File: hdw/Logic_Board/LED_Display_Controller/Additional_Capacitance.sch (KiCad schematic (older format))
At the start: 3 parts

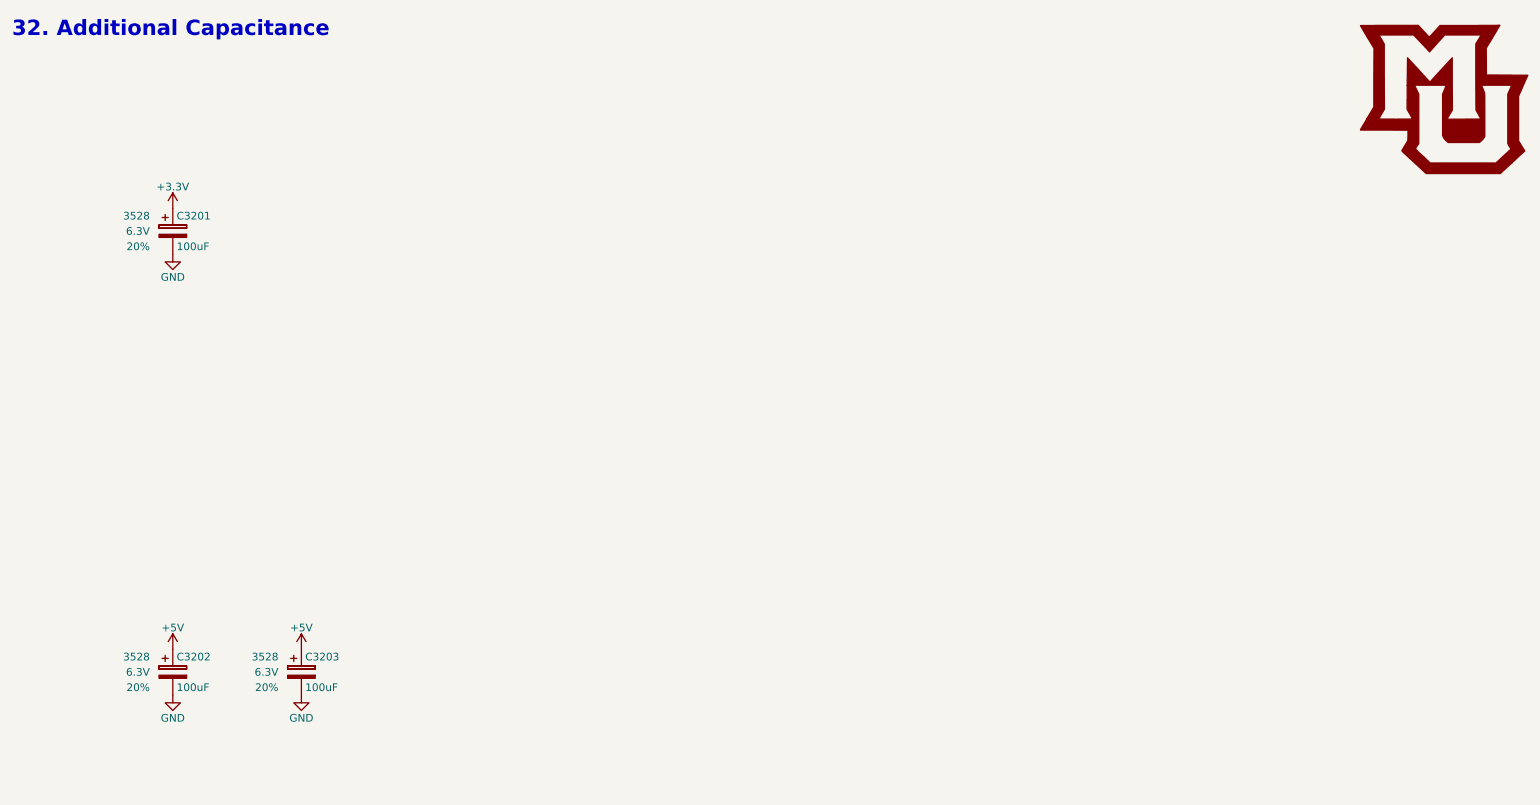
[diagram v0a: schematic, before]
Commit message: Added stitching caps, mor erouting
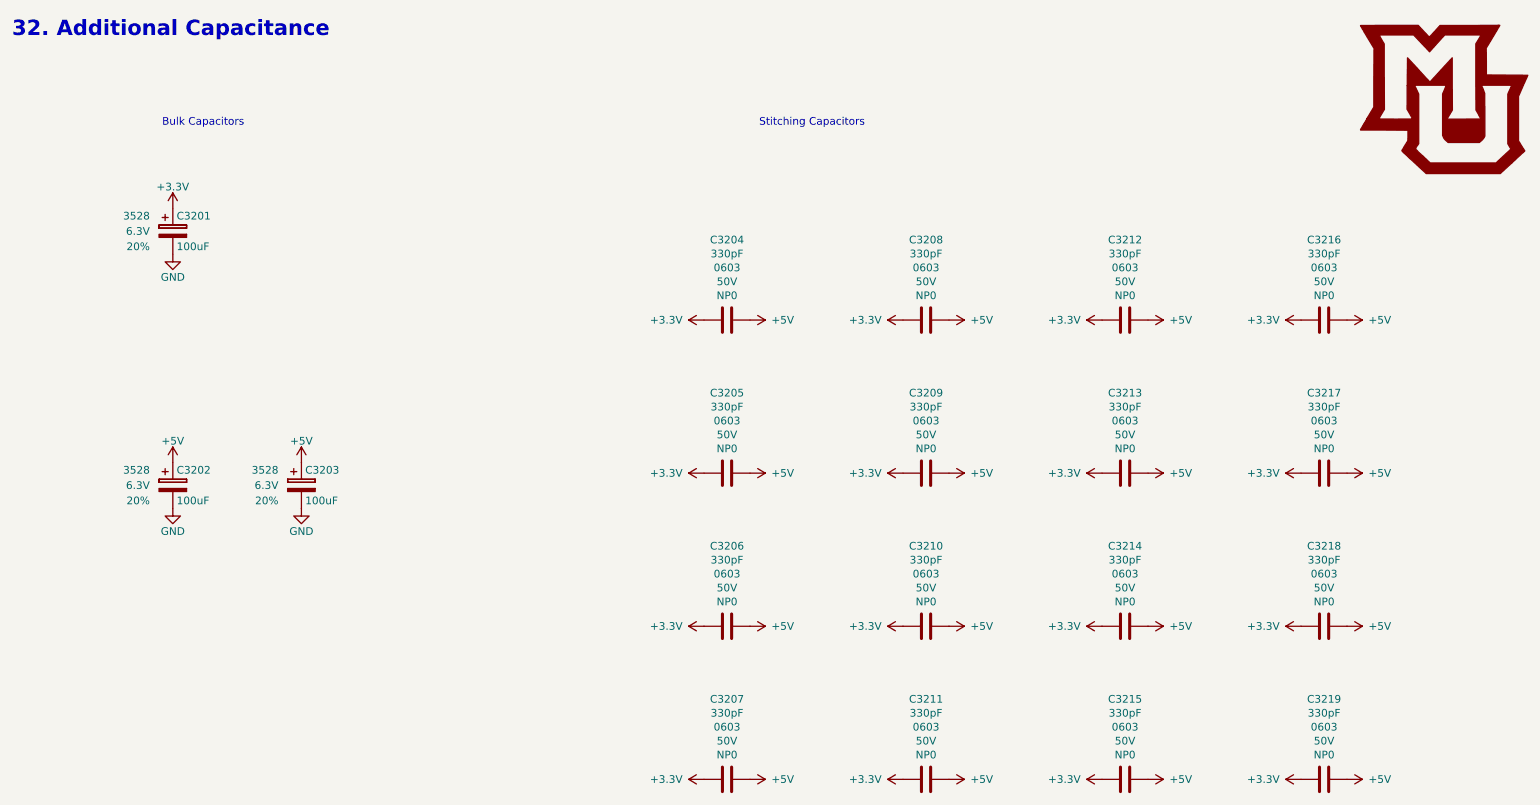
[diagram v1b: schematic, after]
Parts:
- added C3204, C3205, C3206, C3207, C3208, C3209, C3210, C3211, C3212, C3213, C3214, C3215, C3216, C3217, C3218, C3219: 330pF, Capacitors_SMD:C_0603, symbol LED_Display_Local_Library:C_Custom
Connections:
- net +3V3: now also C3204.2, C3205.2, C3206.2, C3207.2, C3208.2, C3209.2, C3210.2, C3211.2, C3212.2, C3213.2, C3214.2, C3215.2, C3216.2, C3217.2, C3218.2, C3219.2
- net +5V: now also C3204.1, C3205.1, C3206.1, C3207.1, C3208.1, C3209.1, C3210.1, C3211.1, C3212.1, C3213.1, C3214.1, C3215.1, C3216.1, C3217.1, C3218.1, C3219.1
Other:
- note added: "Bulk Capacitors"
- note added: "Stitching Capacitors"
- moved on the sheet: C3202, C3203
